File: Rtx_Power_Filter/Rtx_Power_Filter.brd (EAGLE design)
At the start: 118.1 x 47 mm, 22 parts

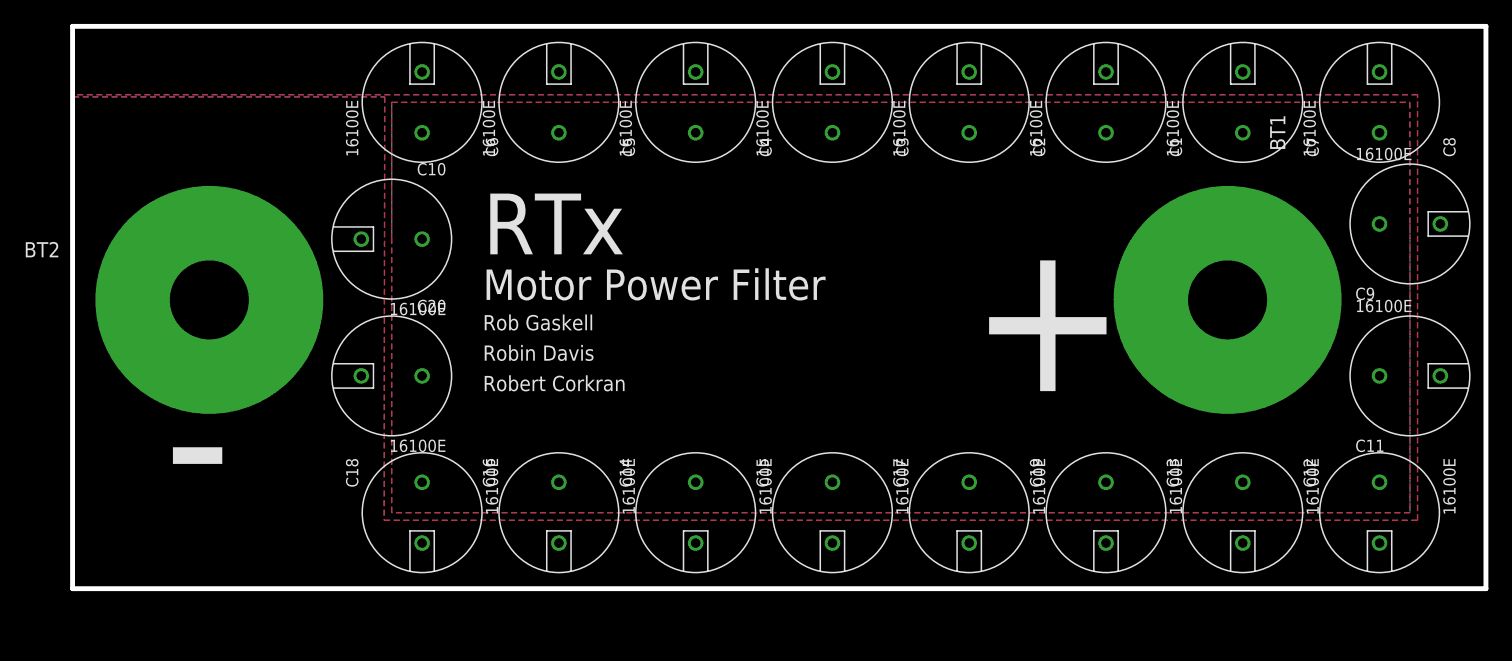
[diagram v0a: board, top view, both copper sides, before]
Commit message: Completed RTx Power Filter Board.
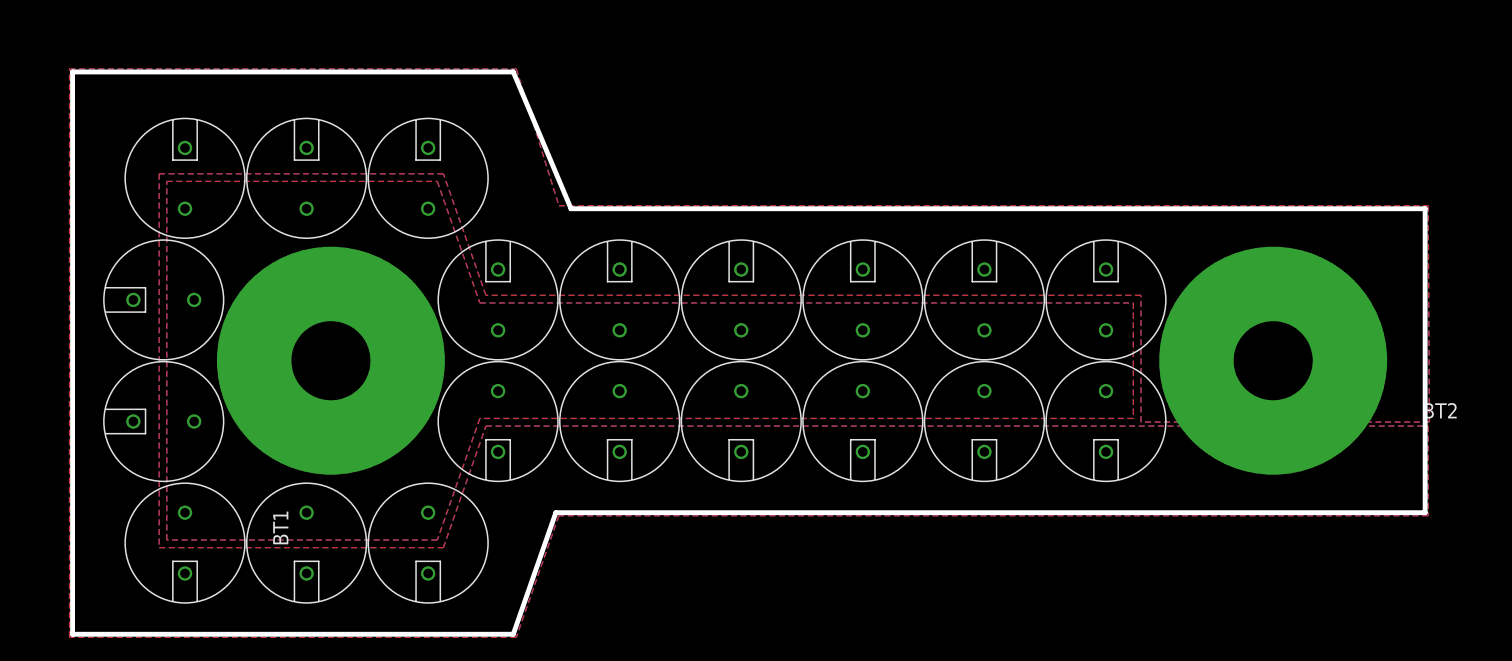
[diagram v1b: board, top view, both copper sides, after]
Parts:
- moved C8 106.4 mm to (9.40, 7.62), turned to 270 degrees
- moved C9 105.4 mm to (7.62, 17.8), turned to 180 degrees
- moved C11 104.3 mm to (7.62, 27.9), turned to 180 degrees
- moved C12 103.7 mm to (9.40, 38.1), turned to 90 degrees
- moved BT2 89.0 mm to (100.3, 22.9), turned to 180 degrees
- moved C7 86.5 mm to (19.6, 7.62), turned to 270 degrees
- moved C13 83.1 mm to (19.6, 38.1), turned to 90 degrees
- moved BT1 75.1 mm to (21.6, 22.9), turned to 90 degrees
- moved C1 67.6 mm to (29.7, 7.62), turned to 270 degrees
- moved C19 63.2 mm to (29.7, 38.1), turned to 90 degrees
- moved C10 61.6 mm to (86.4, 17.8), turned to 270 degrees
- moved C20 60.0 mm to (86.4, 27.9), turned to 90 degrees
- moved C6 54.0 mm to (76.2, 17.8), turned to 270 degrees
- moved C18 50.2 mm to (76.2, 27.9), turned to 90 degrees
- moved C2 47.6 mm to (35.6, 17.8), turned to 270 degrees
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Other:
- board size 118.1 x 47 mm -> 113 x 47 mm
- board text added: "Axis Motor Power Filter"
- board text removed: "Motor Power Filter"
